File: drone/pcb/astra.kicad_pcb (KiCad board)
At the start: 4 copper layers, 44.6 x 44.6 mm, 91 parts, among them J1 Conn_01x02_Pin, J2 Conn_02x11_Odd_Even, J3 Conn_01x04_MountingPin, M1 Motor_DC, M2 Motor_DC, M3 Motor_DC, M4 Motor_DC, Q1 AO3400A, Q2 AO3400A, Q3 AO3400A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

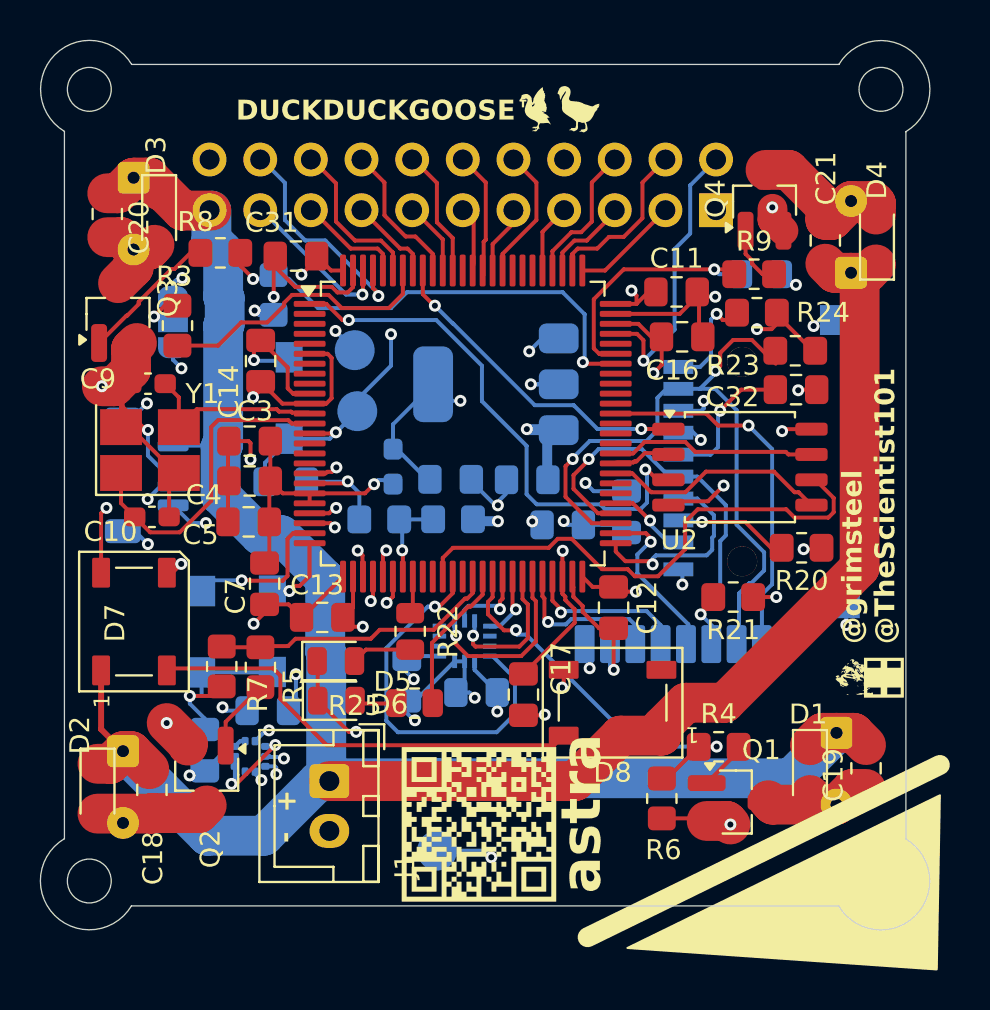
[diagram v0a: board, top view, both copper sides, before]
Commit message: [pcb] add JST FPV connector
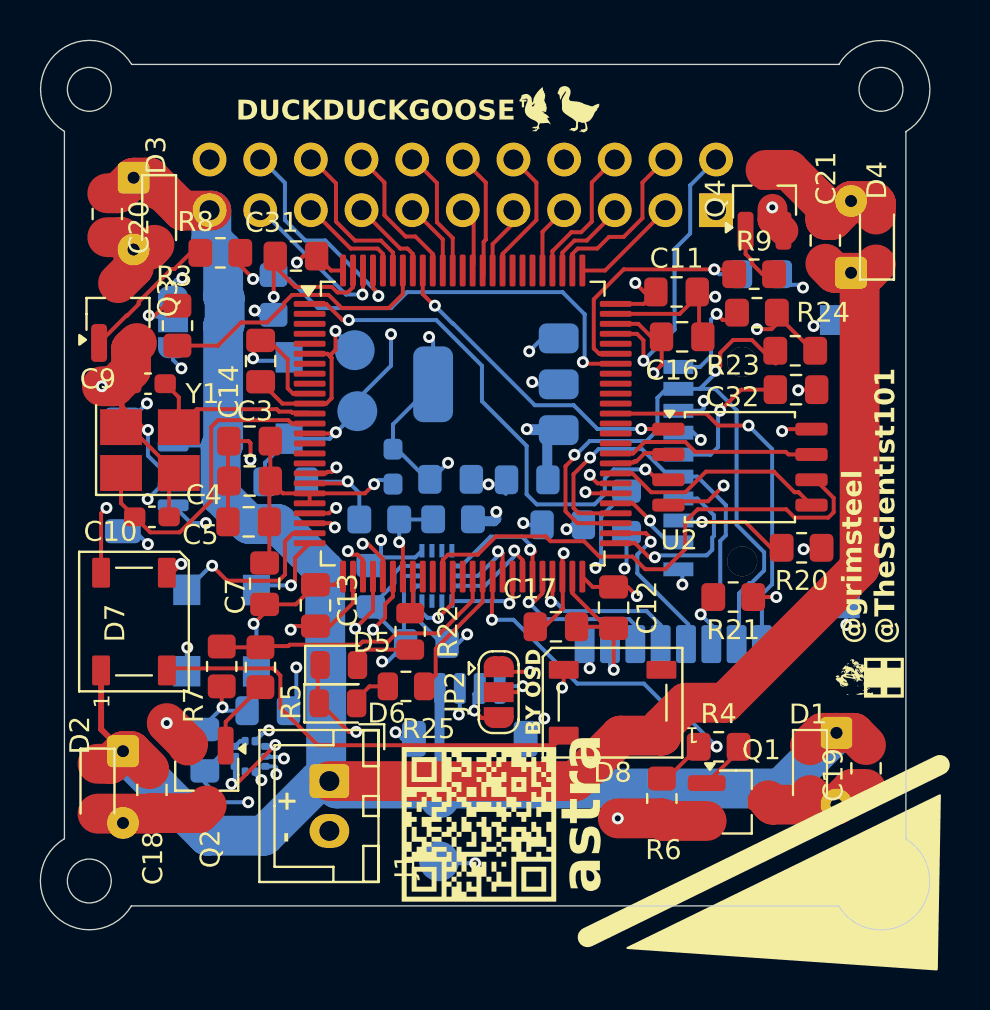
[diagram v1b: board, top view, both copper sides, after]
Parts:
- added J4: Conn_01x04_MountingPin, Connector_JST:JST_SH_BM04B-SRSS-TB_1x04-1MP_P1.00mm_Vertical, B.Cu at (145.0, 69.3)
- added JP2: SolderJumper_3_Open, Jumper:SolderJumper-3_P1.3mm_Open_RoundedPad1.0x1.5mm, F.Cu at (146.4, 68.2)
- moved C30 5.04 mm to (140.0, 62.9)
- moved C17 3.77 mm to (149.3, 64.9), turned to 180 degrees
- moved U7 3.56 mm to (143.3, 62.4), turned to 90 degrees
- moved C29 3.52 mm to (142.8, 65.8)
- moved TP1 1.01 mm to (143.5, 73.5)
- moved R25 0.94 mm to (141.8, 67.9)
- moved SW1 0.80 mm to (134.3, 65.1)
- moved SW3 0.74 mm to (130.8, 65.1)
- moved C13 0.69 mm to (137.2, 63.8), turned to 90 degrees
- moved TP4 0.54 mm to (143.4, 76.7)
- moved D5 0.25 mm to (138.4, 66.8)
- moved D6 0.15 mm to (138.4, 68.8)
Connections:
- U3 pad 56: unconnected-(U3-PD9-Pad56) -> OSD_VOUT
- U3 pad 57: unconnected-(U3-PD10-Pad57) -> OSD_VIN
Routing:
- net +3.3V: track 149.9 -> 73.6 mm, vias 20 -> 21
- net OSD_VIN: track 0.00 -> 19.2 mm, vias 0 -> 2
- net IMU_INT1: track 19.5 -> 3.86 mm
- net OSD_VOUT: track 0.00 -> 14.2 mm, vias 0 -> 2
- net GND: track 124.3 -> 132.7 mm, vias 38 -> 39
- net +BATT: track 173.4 -> 179.1 mm
- net IMU_CS: track 9.07 -> 6.30 mm
- net FPV_VIN: track 0.00 -> 2.54 mm, vias 0 -> 1
- net Net-(C16-Pad2): track 22.5 -> 20.0 mm
- net SPI4_MOSI: track 7.39 -> 5.35 mm
- net BTN2: track 7.73 -> 8.93 mm
- net SPI1_MISO: track 16.6 -> 17.7 mm
- net SPI4_MISO: track 3.40 -> 4.35 mm
- net FLASH_IO_2: track 26.3 -> 25.5 mm
- net STATUS_LED_2: track 7.49 -> 6.72 mm
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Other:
- board text added: "BY OSD"
- board text added: "FPV"
- board text added: "UART"

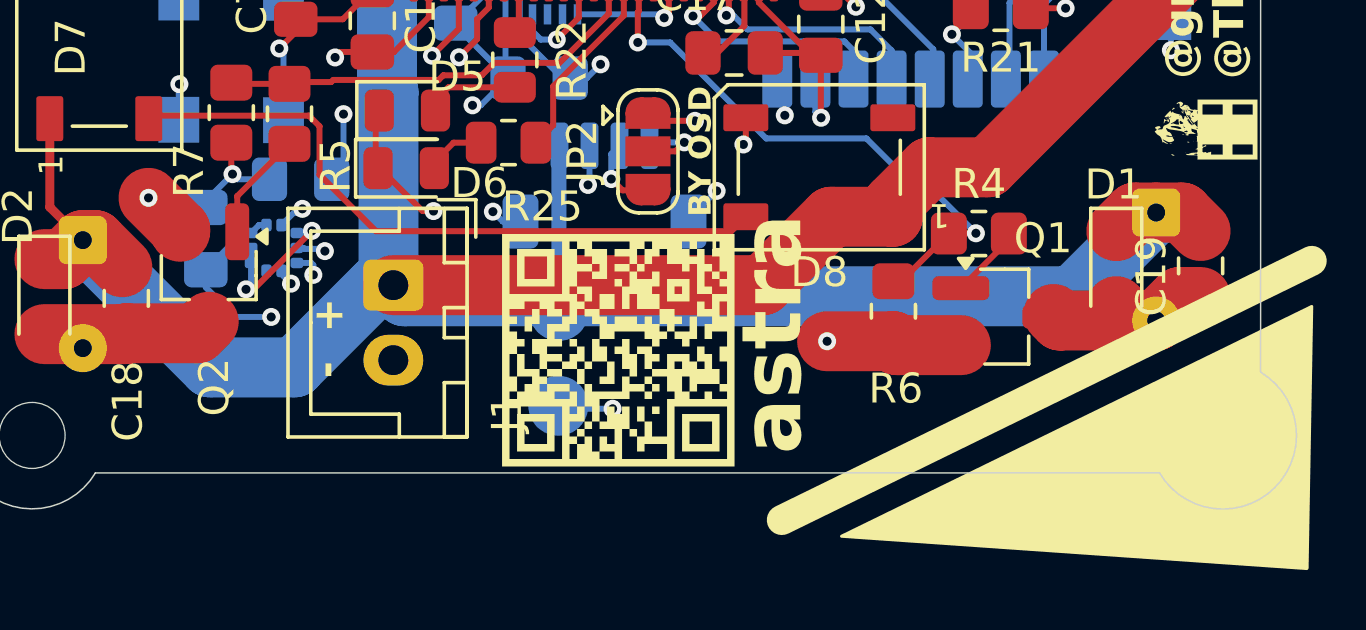
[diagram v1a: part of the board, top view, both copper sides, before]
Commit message: [bom] change battery and [controller] add button 3d files
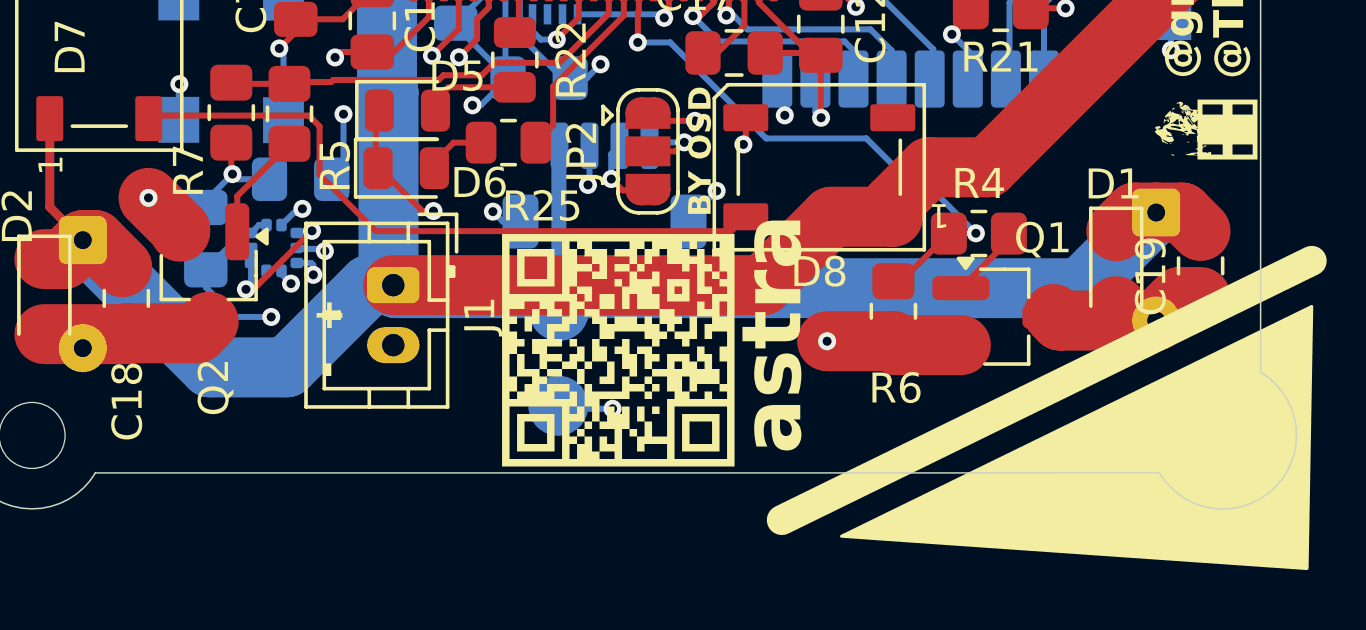
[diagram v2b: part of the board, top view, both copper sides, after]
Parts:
- J1: footprint Connector_JST:JST_XH_B2B-XH-A_1x02_P2.50mm_Vertical -> Connector_JST:JST_PH_B2B-PH-K_1x02_P2.00mm_Vertical

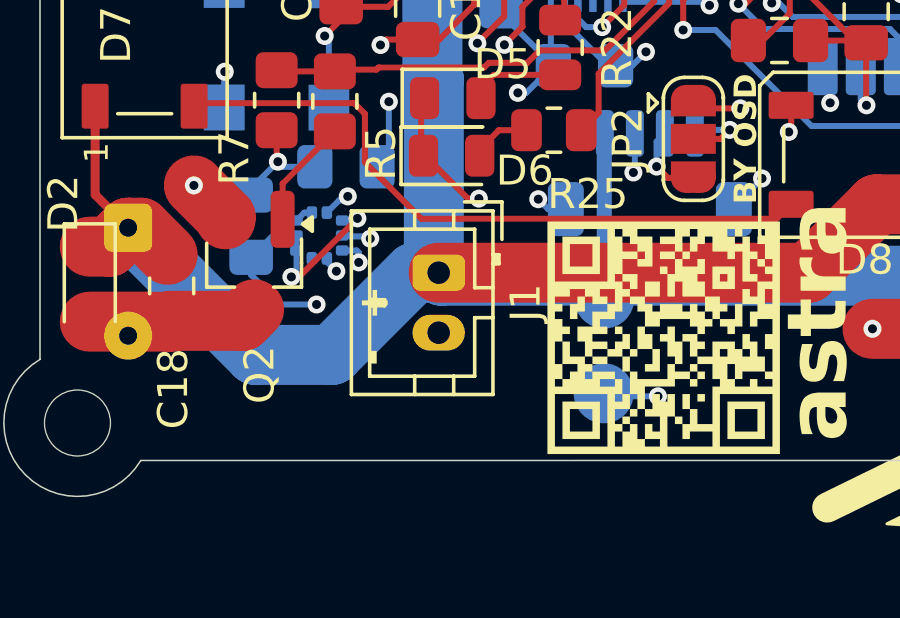
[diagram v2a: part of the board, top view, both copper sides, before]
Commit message: [pcb] update battery connector footprint
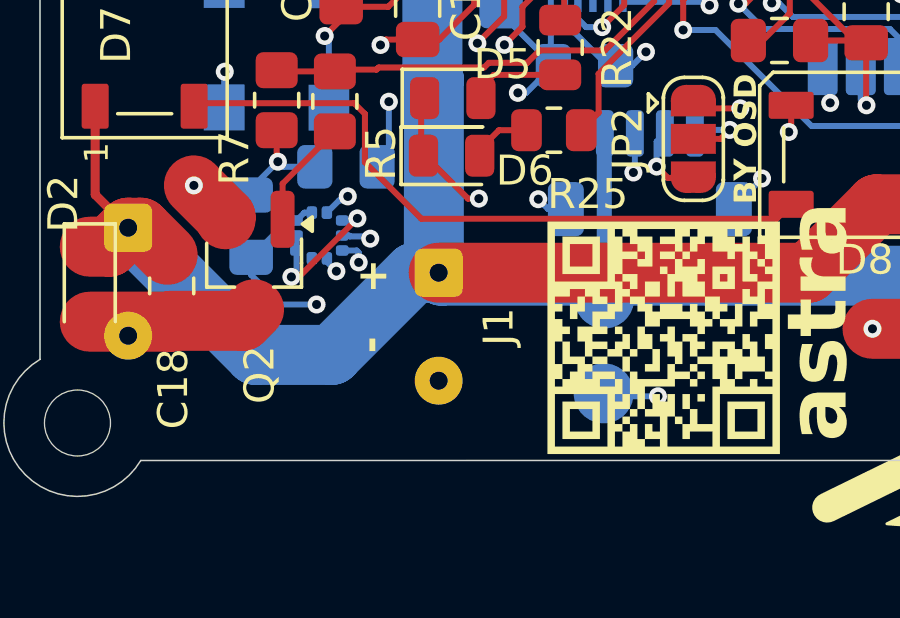
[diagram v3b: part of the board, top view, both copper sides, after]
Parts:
- J1: footprint Connector_JST:JST_PH_B2B-PH-K_1x02_P2.00mm_Vertical -> Connector_Wire:SolderWire-0.1sqmm_1x02_P3.6mm_D0.4mm_OD1mm

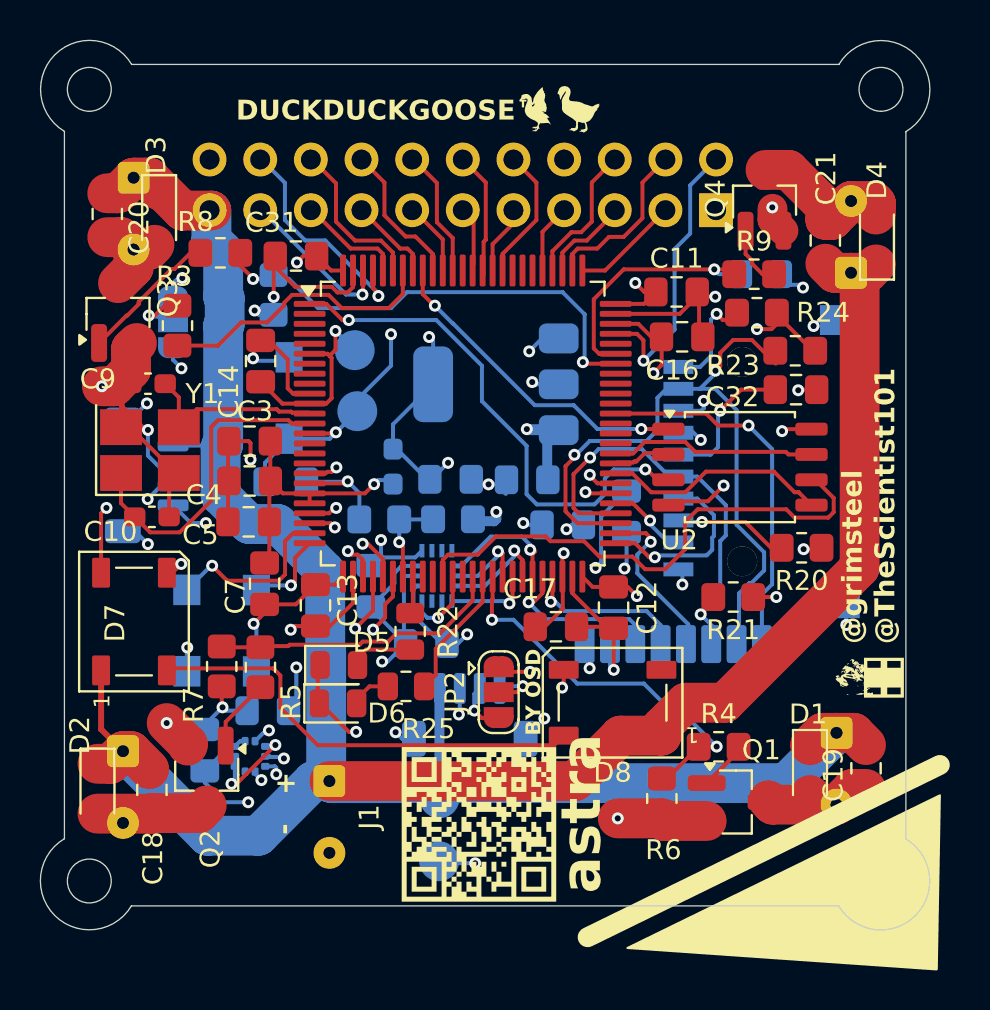
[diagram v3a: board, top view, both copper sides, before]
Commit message: [pcb] minor routing improvements
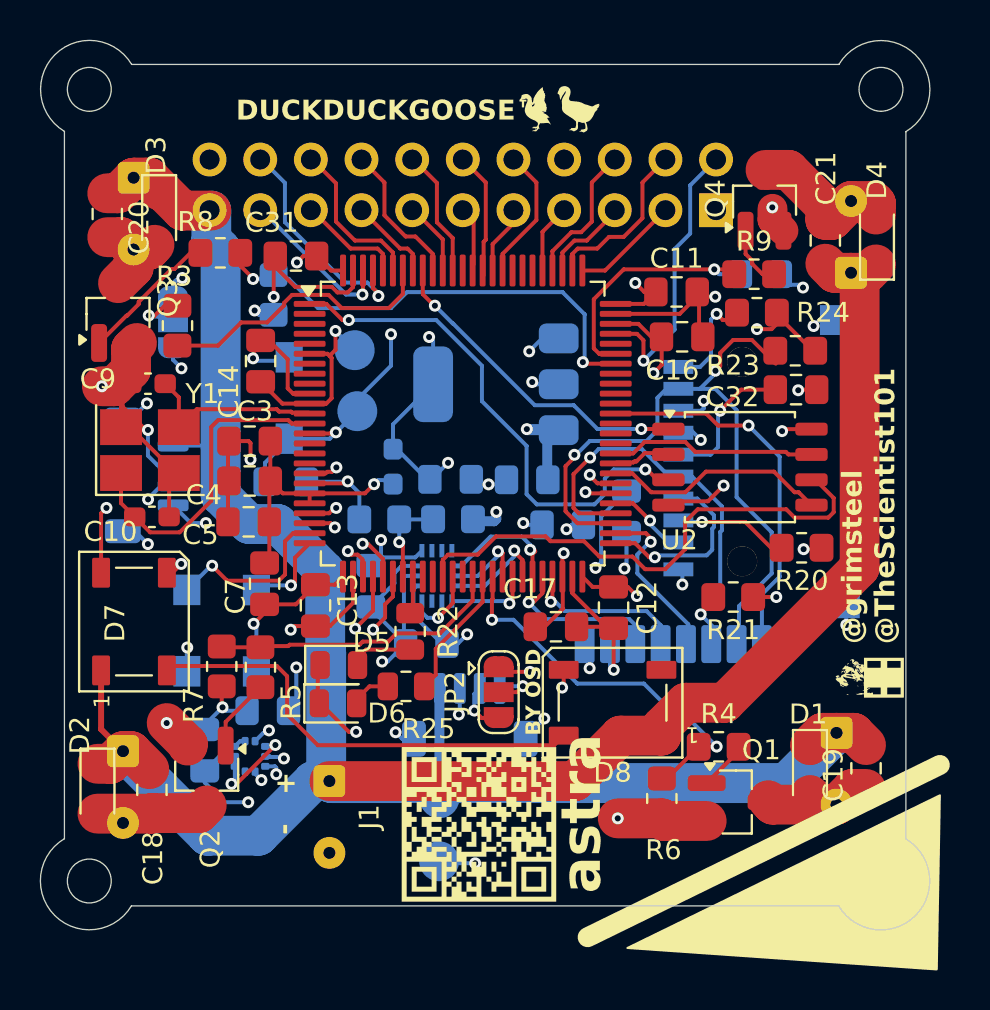
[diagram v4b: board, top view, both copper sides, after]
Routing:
- net GND: track 132.7 -> 132.0 mm

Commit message: [pcb] manufacturing constraints and cleanup
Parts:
- moved C16 0.24 mm to (155.4, 50.3)
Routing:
- net GND: track 132.0 -> 126.1 mm
- net +3.3V: track 73.6 -> 71.0 mm
- net DDG_MAGIC_7: track 3.46 -> 2.80 mm
- net BTN1: track 4.61 -> 4.00 mm
- net RST: track 26.0 -> 25.5 mm
- net UART4_RX: track 12.9 -> 12.3 mm
- net BAR_CS: track 16.0 -> 15.4 mm
- net SD_CD: track 4.06 -> 3.55 mm
- net Net-(C16-Pad2): track 19.7 -> 19.2 mm

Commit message: [pcb] update commit silkscreen
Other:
- board text added: "09fc4c9"
- board text removed: "0123abc"
